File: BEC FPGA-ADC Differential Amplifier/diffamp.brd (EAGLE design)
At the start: 80 x 100 mm, 16 parts, among them U1 ADA4807-2ARMZRM_8-M

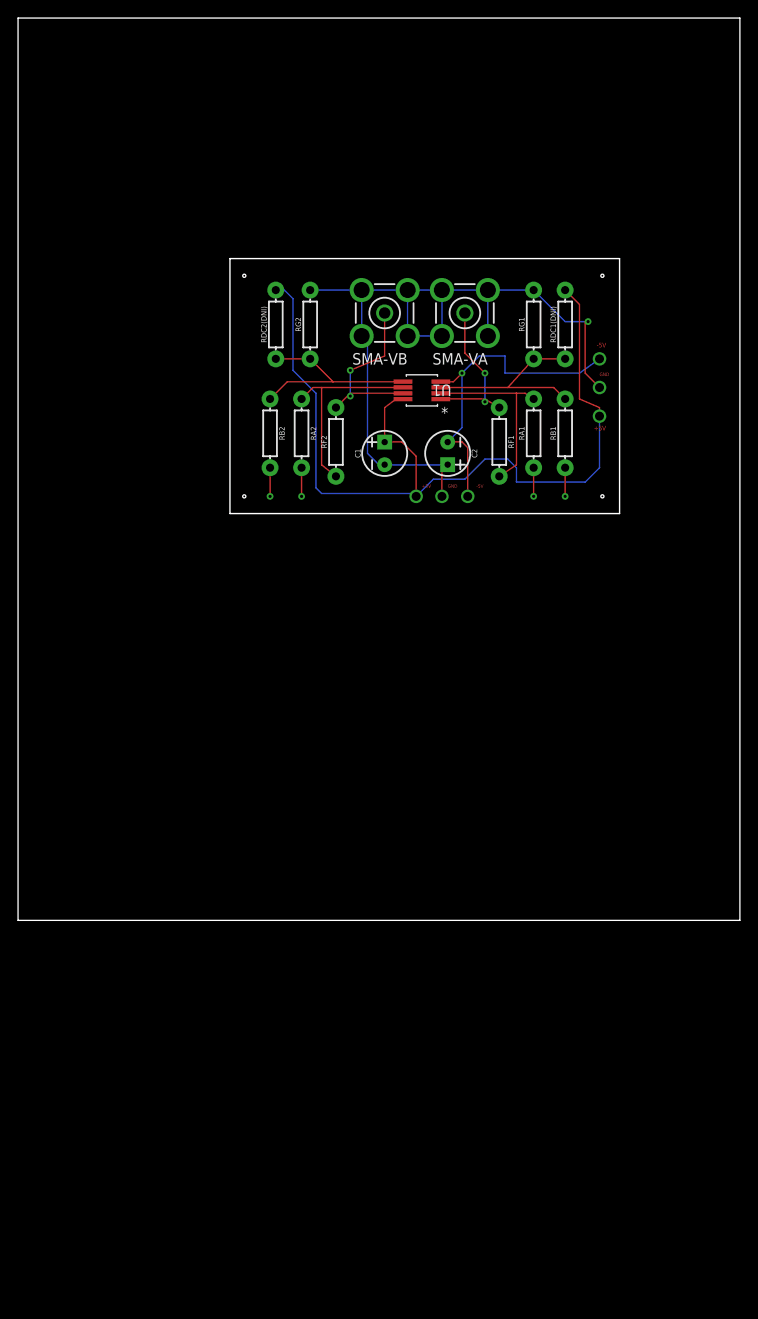
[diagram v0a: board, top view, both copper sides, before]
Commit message: Updated differential amplifier circuit. About to begin rewiring. Also removing extra connectors, single port access and that's all.
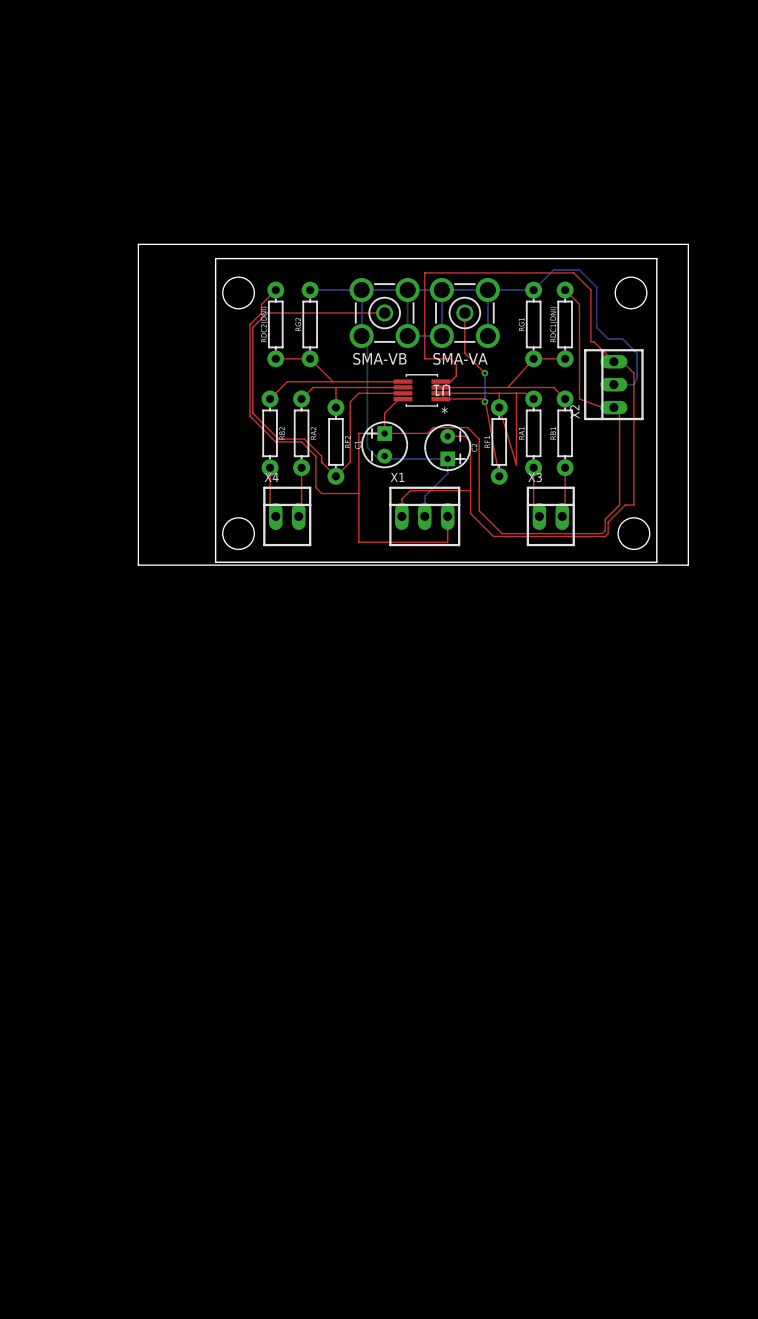
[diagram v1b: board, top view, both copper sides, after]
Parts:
- removed FRAME1: FRAME-LETTER, SparkFun-Aesthetics:CREATIVE_COMMONS
- added X1, X2: 22-23-2031, con-molex:22-23-2031
- added X3, X4: 22-23-2021, con-molex:22-23-2021
- moved C1 0.95 mm to (51.4, 39.4)
- moved C2 0.64 mm to (58.4, 39.1)
- turned RF1 to 90 degrees
- turned RF2 to 270 degrees
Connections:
- net +5V: now also X1.3, X2.1
- net -5V: now also X1.1, X2.3
- net DAC-A1: now also X3.1
- net DAC-A2: now also X3.2
- net DAC-B1: now also X4.2
- net DAC-B2: now also X4.1
- net GND: now also X1.2, X2.2
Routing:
- net -5V: track 37.5 -> 104.5 mm, vias 3 -> 0
- net +5V: track 97.6 -> 130.9 mm, vias 2 -> 0
- net VOUT2: track 19.7 -> 52.3 mm, vias 2 -> 0
- net GND: track 91.1 -> 102.9 mm, vias 3 -> 0
- net -IN2: track 21.9 -> 13.5 mm
- net VOUT1: track 17.4 -> 24.2 mm
- net -IN1: track 20.6 -> 26.5 mm
- net DAC-A1: track 3.17 -> 5.66 mm, vias 1 -> 0
- net DAC-B2: track 3.17 -> 5.66 mm, vias 1 -> 0
- net DAC-B1: track 3.17 -> 5.53 mm, vias 1 -> 0
- net DAC-A2: track 3.17 -> 5.53 mm, vias 1 -> 0
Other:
- board size 80 x 100 mm -> 61 x 35.5 mm
- board text removed: "+5V"
- board text removed: "-5V"
- board text removed: "GND"

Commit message: Added new source capacitors.
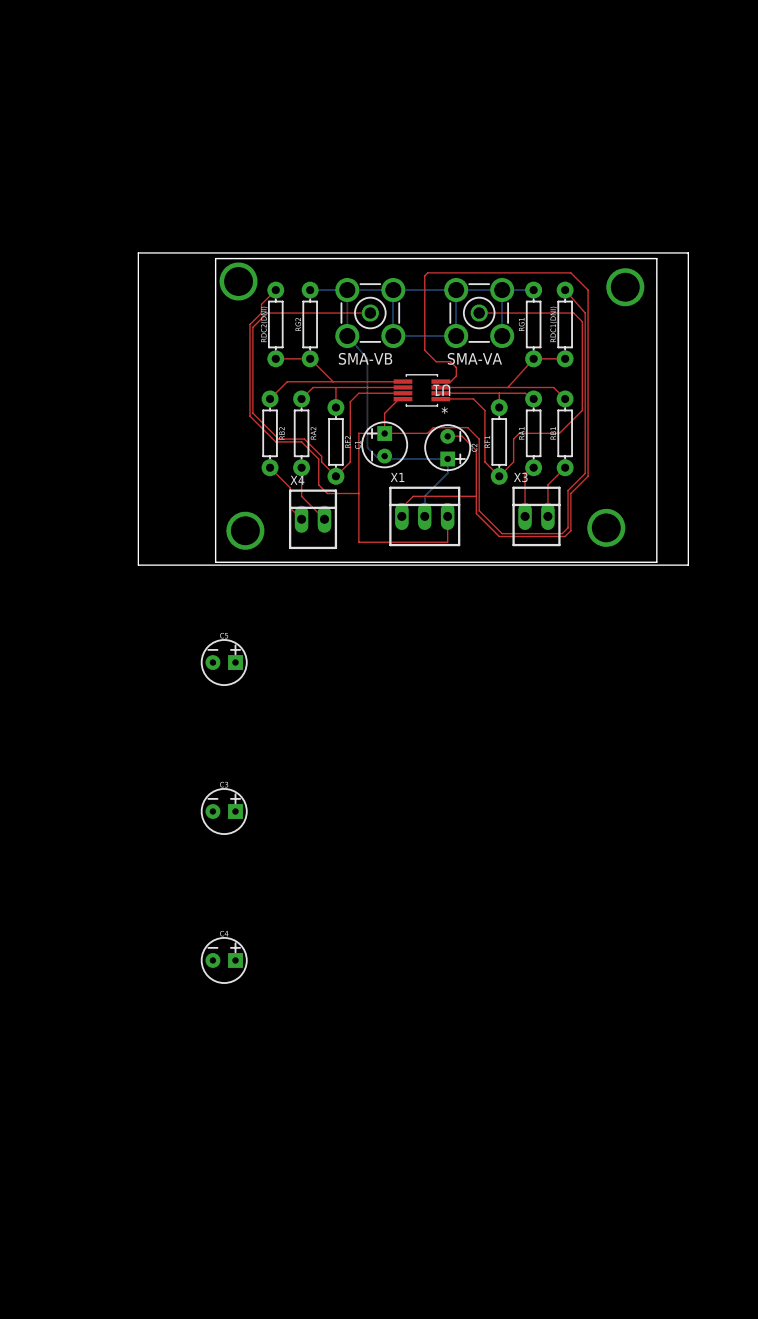
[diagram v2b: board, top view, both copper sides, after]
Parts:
- removed X2: 22-23-2031, con-molex:22-23-2031
- added C3, C4: 0.1uF, SparkFun-Capacitors:CPOL-RADIAL-2.5MM-5MM
- added C5: 10nF, SparkFun-Capacitors:CPOL-RADIAL-2.5MM-5MM
- moved X4 2.88 mm to (43.5, 31.1)
- moved SMA-VB 1.59 mm to (49.8, 54.0)
- moved SMA-VA 1.59 mm to (61.9, 54.0)
- moved X3 1.59 mm to (68.3, 31.4)
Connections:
- net +5V: now also C4.1, C5.1; no longer X2.1
- net -5V: now also C3.2, C5.2; no longer X2.3
- net GND: now also C3.1, C4.2; no longer X2.2
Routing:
- net VOUT1: track 24.2 -> 48.6 mm, vias 2 -> 0
- net GND: track 102.9 -> 82.1 mm
- net -IN1: track 26.5 -> 11.9 mm
- net -5V: track 104.5 -> 94.2 mm
- net +5V: track 130.9 -> 123.2 mm
- net VOUT2: track 52.3 -> 50.7 mm
- net DAC-B2: track 5.66 -> 7.16 mm
- net DAC-B1: track 5.53 -> 6.77 mm
- net DAC-A2: track 5.53 -> 6.19 mm
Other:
- board size 61 x 35.5 mm -> 61 x 34.6 mm

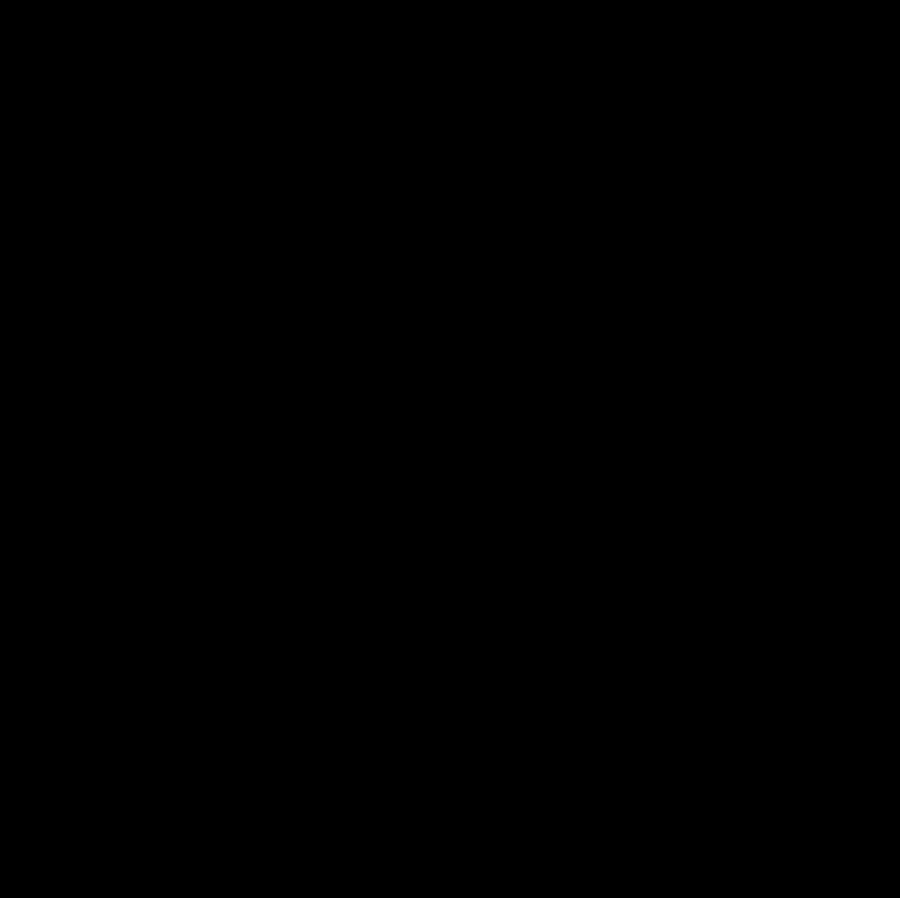
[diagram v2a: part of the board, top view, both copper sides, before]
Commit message: Added output series resistance. Not Routed
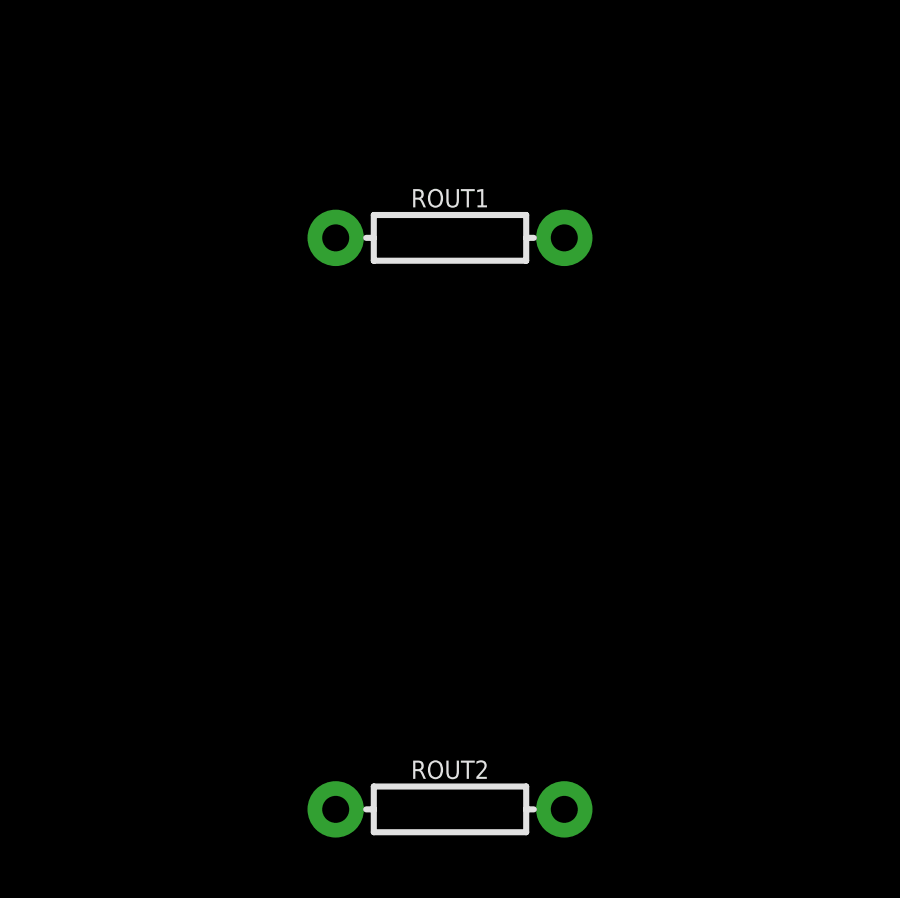
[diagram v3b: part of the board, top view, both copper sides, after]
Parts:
- added ROUT1, ROUT2: 0, SparkFun-Resistors:AXIAL-0.3
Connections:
- net VOUT1: now also ROUT1.P$1, ROUT1.P$2
- net VOUT2: now also ROUT2.P$1, ROUT2.P$2
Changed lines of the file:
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@@
 <attribute name="PROD_ID" value="CAP-08440" x="33.655" y="-17.78" size="1.778" layer="27" display="off"/>
+</element>
+<element name="ROUT1" library="SparkFun-Resistors" package="AXIAL-0.3" value="0" x="37.465" y="-35.56">
+<attribute name="PROD_ID" value=" " x="37.465" y="-35.56" size="1.778" layer="27" display="off"/>
+</element>
+<element name="ROUT2" library="SparkFun-Resistors" package="AXIAL-0.3" value="0" x="37.465" y="-54.61">
+<attribute name="PROD_ID" value=" " x="37.465" y="-54.61" size="1.778" layer="27" display="off"/>
 </element>
 </elements>
@@
 <wire x1="73.3425" y1="53.0225" x2="72.39" y2="53.975" width="0.1524" layer="1"/>
 <wire x1="72.39" y1="53.975" x2="61.9125" y2="53.975" width="0.1524" layer="1"/>
+<contactref element="ROUT1" pad="P$1"/>
+<contactref element="ROUT1" pad="P$2"/>
 <wire x1="57.785" y1="44.45" x2="57.658" y2="44.4275" width="0" layer="19" extent="1-1"/>
+<wire x1="41.275" y1="-35.56" x2="64.135" y2="35.8775" width="0" layer="19" extent="1-1"/>
+<wire x1="33.655" y1="-35.56" x2="41.275" y2="-35.56" width="0" layer="19" extent="1-1"/>
 </signal>
 <signal name="GND">
@@
 <wire x1="47.625" y1="44.1325" x2="47.625" y2="37.465" width="0.1524" layer="1"/>
 <wire x1="47.625" y1="44.1325" x2="48.5775" y2="45.085" width="0.1524" layer="1"/>
+<contactref element="ROUT2" pad="P$1"/>
+<contactref element="ROUT2" pad="P$2"/>
 <wire x1="53.34" y1="45.085" x2="53.467" y2="45.0775" width="0" layer="19" extent="1-1"/>
+<wire x1="41.275" y1="-54.61" x2="46.0375" y2="35.8775" width="0" layer="19" extent="1-1"/>
+<wire x1="33.655" y1="-54.61" x2="41.275" y2="-54.61" width="0" layer="19" extent="1-1"/>
 </signal>
 <signal name="-IN2">

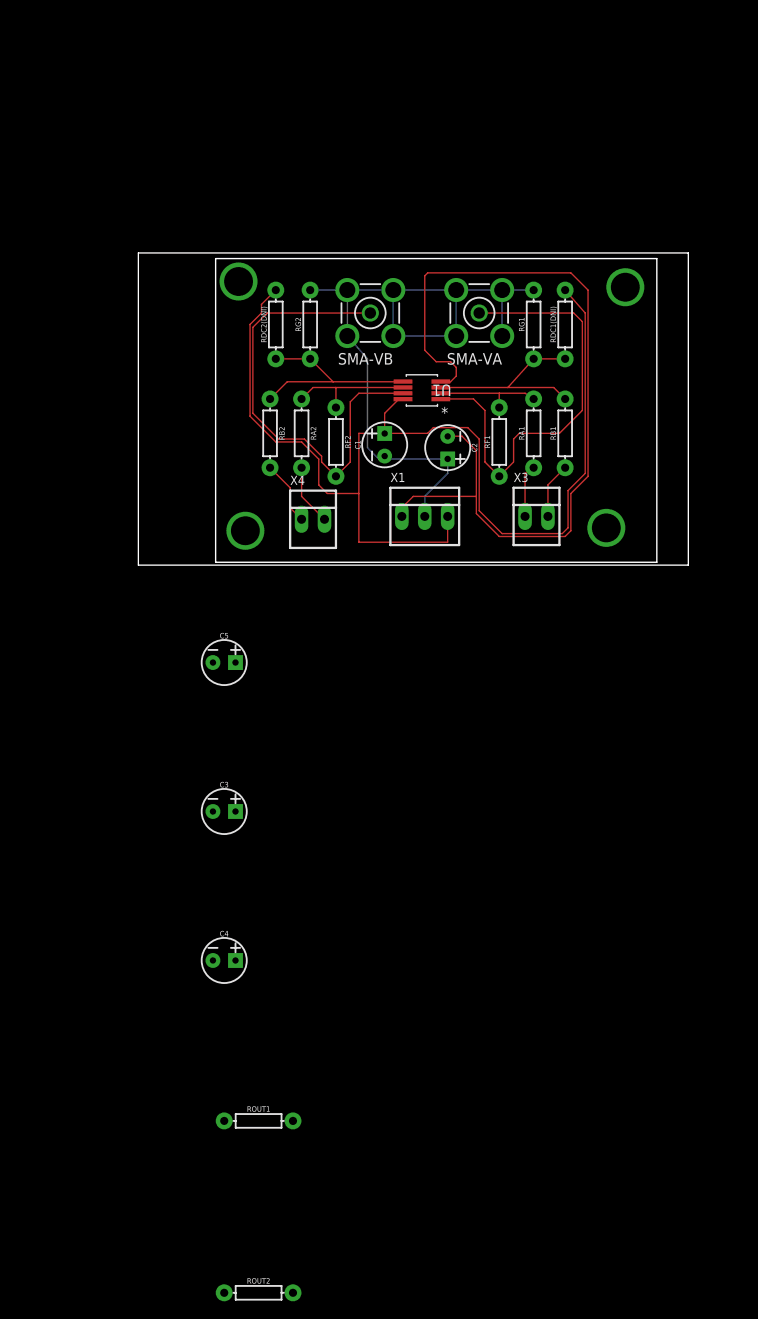
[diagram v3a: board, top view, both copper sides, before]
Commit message: Added ground plane and zero ohm resistors. Board Layout modified.
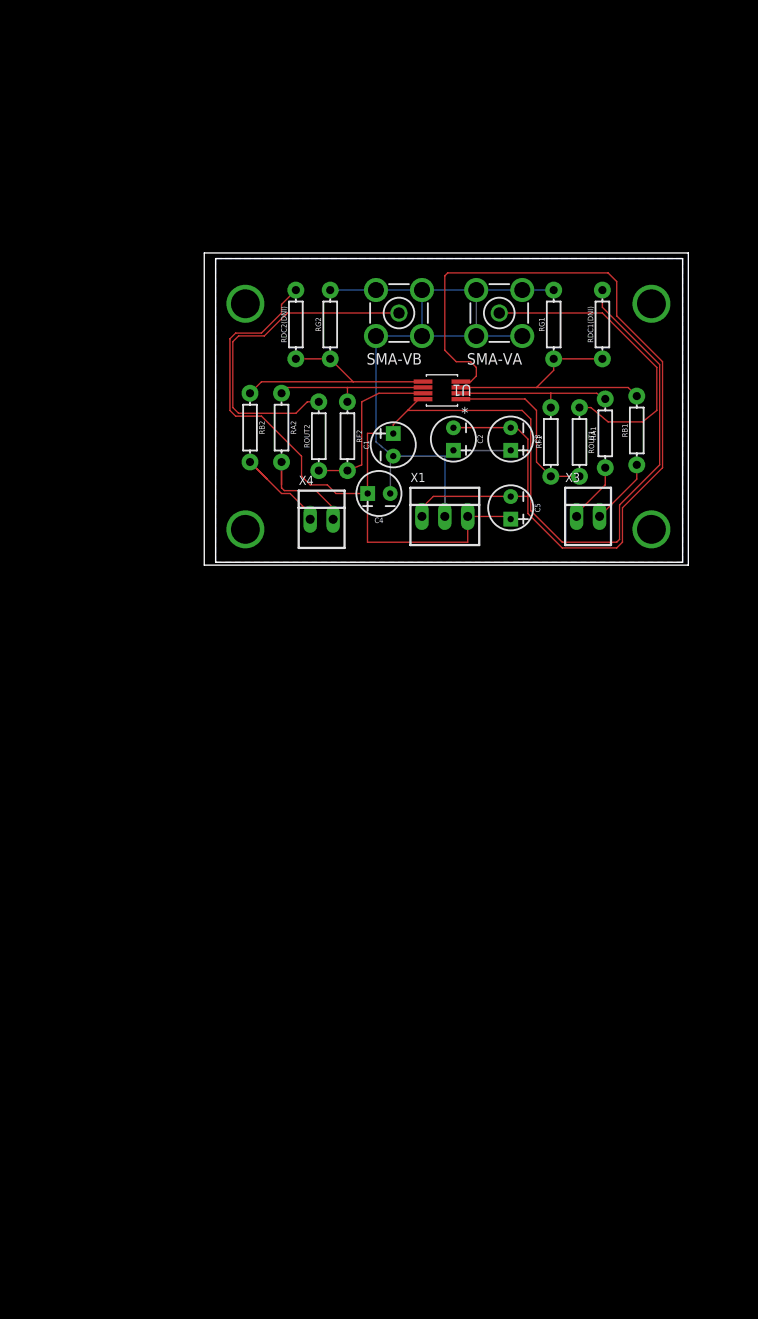
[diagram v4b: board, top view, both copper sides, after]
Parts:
- moved ROUT2 95.2 mm to (44.1, 40.3), turned to 90 degrees
- moved ROUT1 83.2 mm to (73.0, 39.7), turned to 270 degrees
- moved C4 54.5 mm to (50.8, 34.0), turned to 180 degrees
- moved C3 52.1 mm to (65.4, 40.0), turned to 270 degrees
- moved C5 36.1 mm to (65.4, 32.4), turned to 270 degrees
- moved RB1 7.94 mm to (79.4, 41.0)
- moved RA1 7.94 mm to (75.9, 40.6)
- moved X3 5.72 mm to (74.0, 31.4)
- moved RF1 5.71 mm to (69.8, 39.7)
- moved RDC1(DNI) 4.13 mm to (75.6, 52.7)
- moved SMA-VB 3.18 mm to (53.0, 54.0)
- moved RA2 2.31 mm to (40.0, 41.3)
- moved RB2 2.31 mm to (36.5, 41.3)
- moved RG1 2.22 mm to (70.2, 52.7)
- moved RDC2(DNI) 2.22 mm to (41.6, 52.7)
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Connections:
- new net VSMA1: ROUT1.P$1, SMA-VA.1
- new net VSMA2: ROUT2.P$2, SMA-VB.1
- net VOUT1: no longer ROUT1.P$1, SMA-VA.1
- net VOUT2: no longer ROUT2.P$2, SMA-VB.1
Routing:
- net VSMA2: track 0.00 -> 37.3 mm
- net VSMA1: track 0.00 -> 34.3 mm
- net VOUT2: track 50.7 -> 18.8 mm
- net VOUT1: track 48.6 -> 19.9 mm
- net +5V: track 123.2 -> 145.2 mm
- net -5V: track 94.2 -> 110.3 mm
- net GND: track 82.1 -> 91.8 mm, vias 0 -> 4
- net +IN1: track 21.9 -> 29.1 mm
- net DAC-B1: track 6.77 -> 13.3 mm
- net -IN1: track 11.9 -> 17.7 mm
- net DAC-B2: track 7.16 -> 12.4 mm
- net +IN2: track 22.2 -> 26.3 mm
- net -IN2: track 13.5 -> 17.1 mm
- net DAC-A2: track 6.19 -> 7.42 mm
- net DAC-A1: track 5.91 -> 6.71 mm
- added copper zone on layer 16, net GND
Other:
- board size 61 x 34.6 mm -> 53.6 x 34.6 mm
